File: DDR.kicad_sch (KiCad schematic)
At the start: 62 parts, among them U1 XC7Z020-2CLG484I, U2 MT41K256M16TW, U3 TPS51200DRCR, U4 MT41K256M16TW

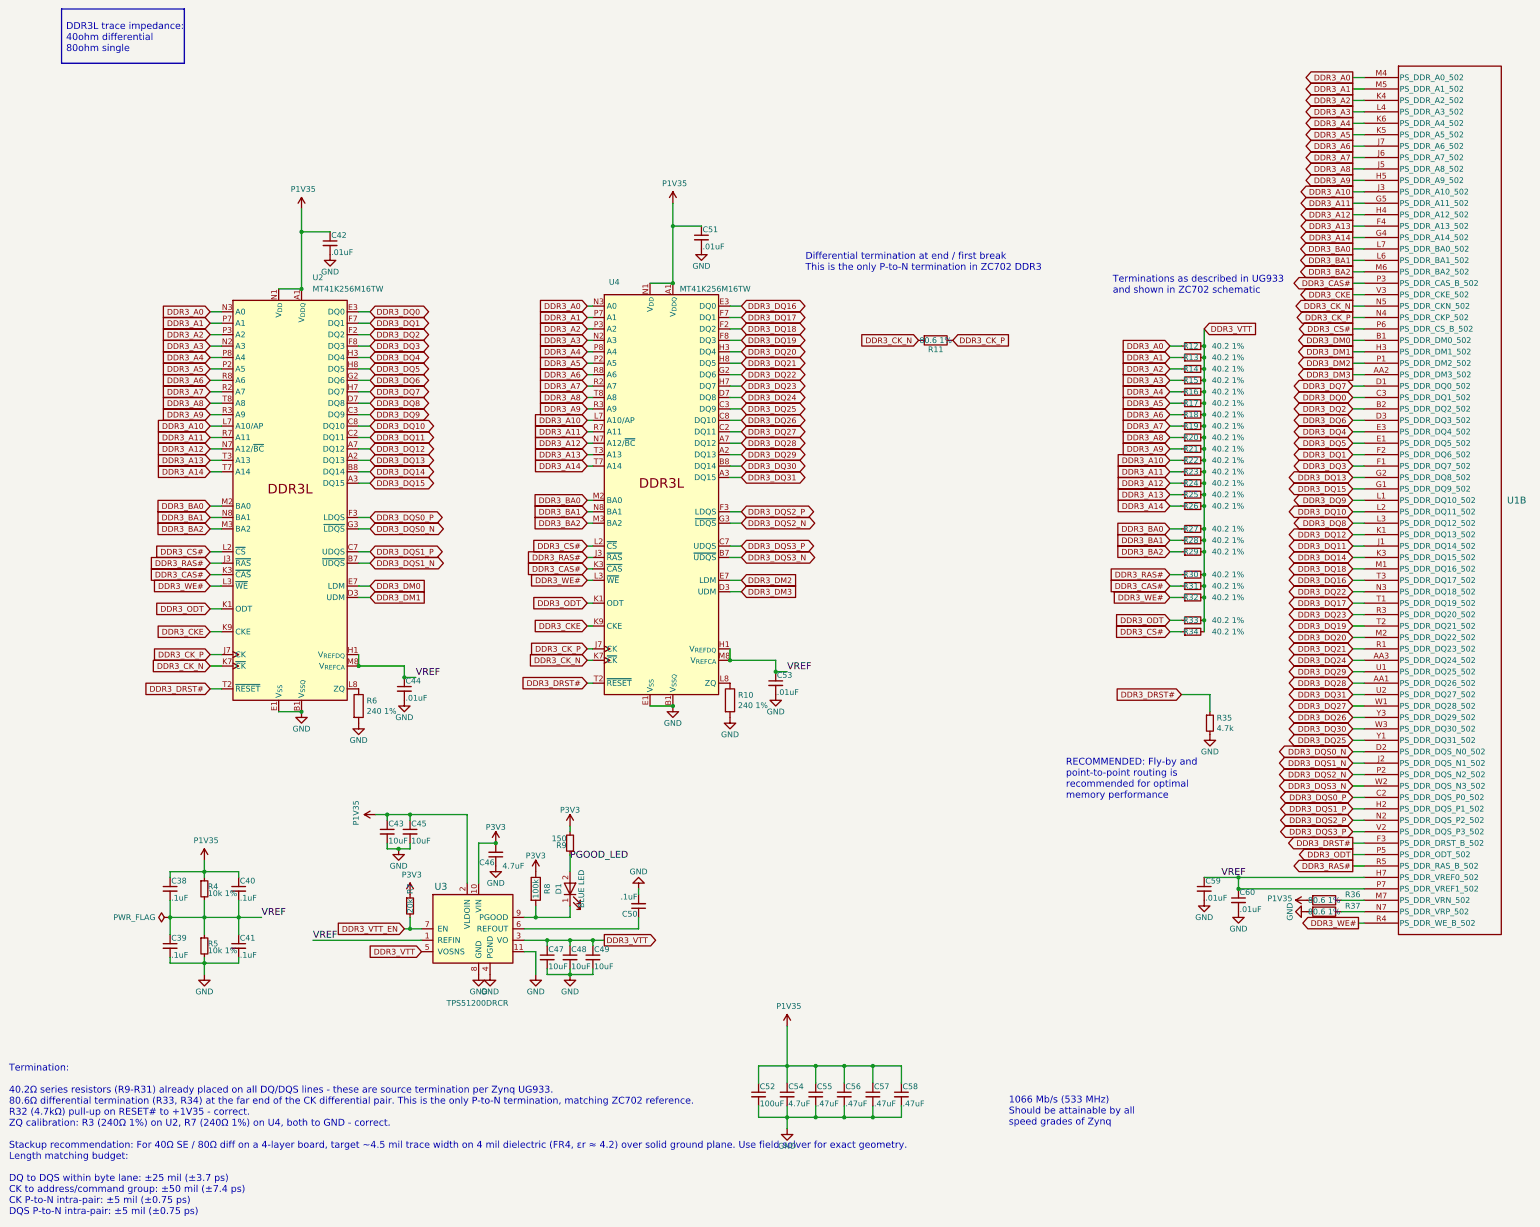
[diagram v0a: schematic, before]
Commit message: updated layouts, added motor
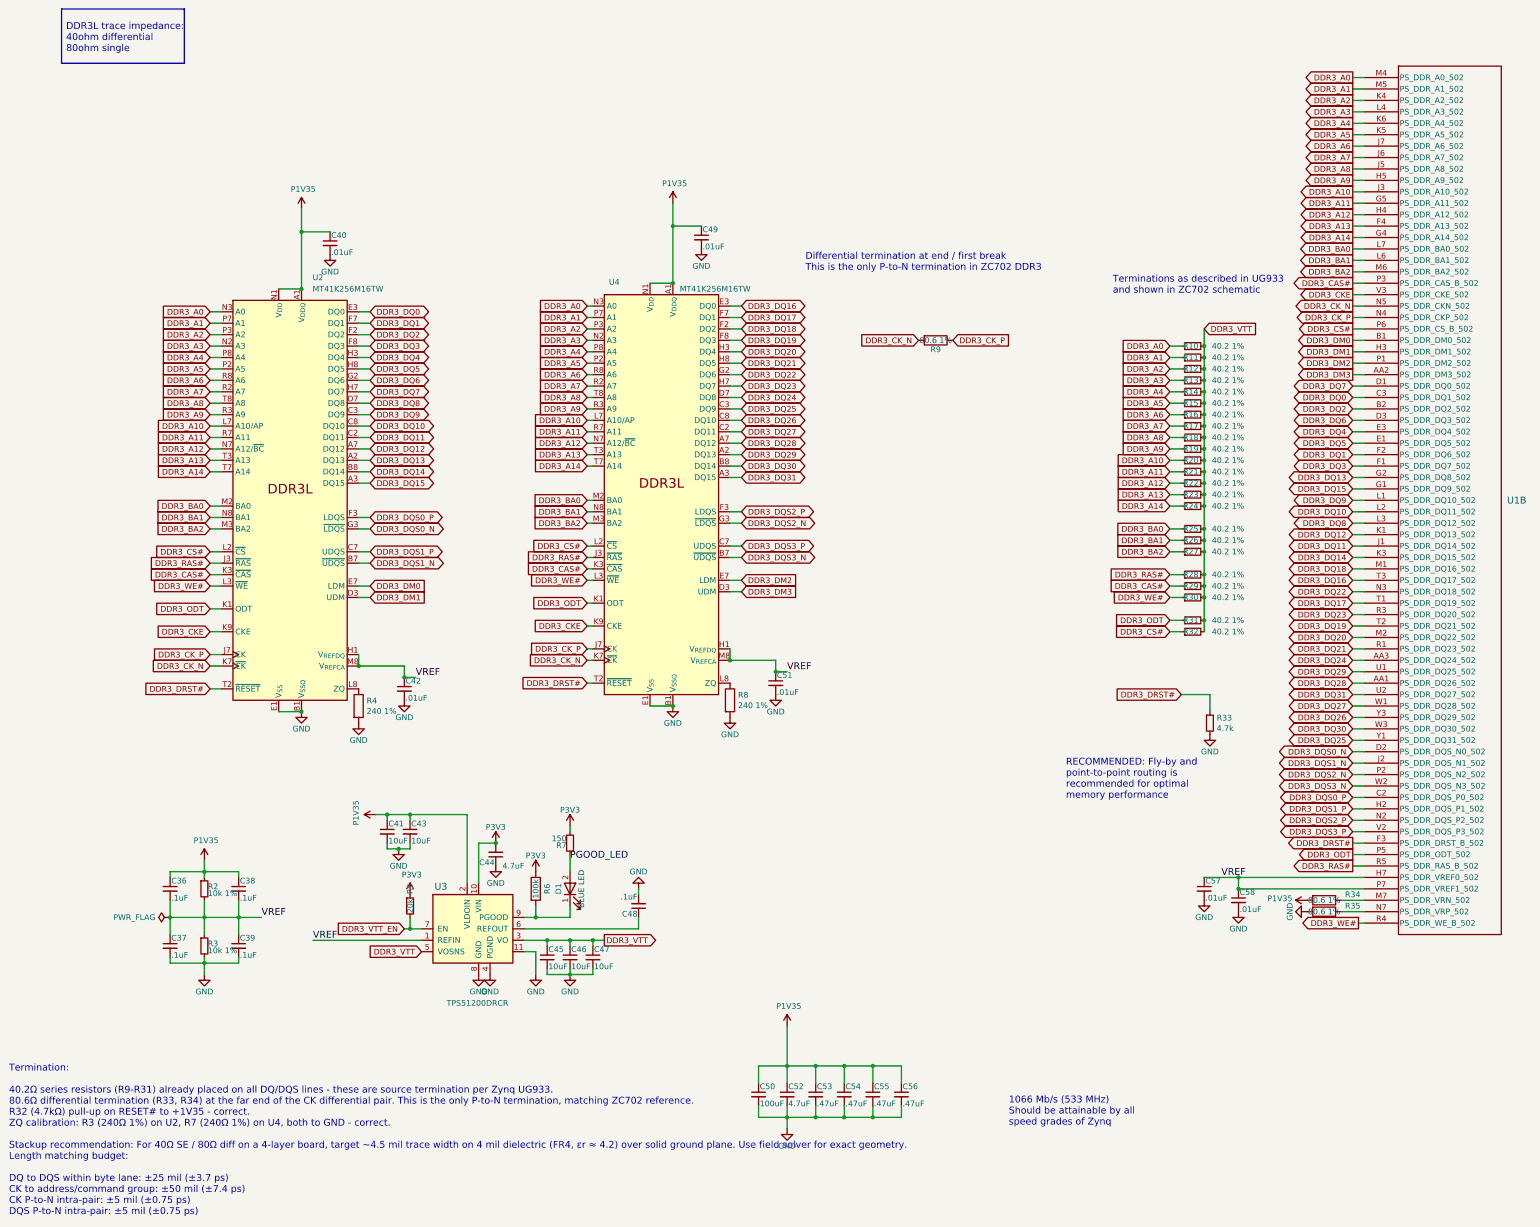
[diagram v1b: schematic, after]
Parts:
- renumbered C38 to C36, C39 to C37, C40 to C38, C41 to C39, C42 to C40, C43 to C41, C44 to C42, C45 to C43, C46 to C44, C47 to C45, C48 to C46, C49 to C47, C50 to C48, C51 to C49, C52 to C50, C53 to C51, C54 to C52, C55 to C53, C56 to C54, C57 to C55, C58 to C56, C59 to C57, C60 to C58, R12 to R10, R13 to R11, R14 to R12, R15 to R13, R16 to R14, R17 to R15, R18 to R16, R19 to R17, R20 to R18, R21 to R19, R4 to R2, R22 to R20, R23 to R21, R24 to R22, R25 to R23, R26 to R24, R27 to R25, R28 to R26, R29 to R27, R30 to R28, R31 to R29, R5 to R3, R32 to R30, R33 to R31, R34 to R32, R35 to R33, R36 to R34, R37 to R35, R6 to R4, R7 to R5, R8 to R6, R9 to R7, R10 to R8, R11 to R9

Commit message: Changes to layout pins
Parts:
- D1: symbol DFTBoard-rescue:LED- -> Device:LED
- U1: footprint DFTcustom:BGA-484_19.0x19.0mm_Layout22x22_P0.80mm_dia0.40mm -> FPGA:BGA-484_19.0x19.0mm_Layout22x22_P0.80mm_dia0.40mm
- U3: symbol tps51200DRCR:TPS51200DRCR -> KiCAD_Library_Cooter:TPS51200DRCR
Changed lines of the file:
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@@
 	(wire
 		(pts
-			(xy 81.28 223.52) (xy 105.41 223.52)
+			(xy 76.2 223.52) (xy 105.41 223.52)
 		)
 		(stroke
@@
 	)
 	(label "VREF"
-		(at 81.28 223.52 0)
+		(at 76.2 223.52 0)
 		(effects
 			(font
@@
 		(dnp no)
 		(property "Reference" "R9"
-			(at 219.71 92.202 90)
+			(at 219.71 88.138 90)
 			(show_name no)
 			(do_not_autoplace no)
@@
 		)
 		(property "Value" "80.6 1%"
-			(at 219.71 90.17 90)
+			(at 219.71 92.202 90)
 			(show_name no)
 			(do_not_autoplace no)
@@
 	)
 	(symbol
-		(lib_id "tps51200DRCR:TPS51200DRCR")
+		(lib_id "KiCAD_Library_Cooter:TPS51200DRCR")
 		(at 118.11 220.98 0)
 		(unit 1)
@@
 	)
 	(symbol
-		(lib_id "DFTBoard-rescue:LED-")
+		(lib_id "Device:LED")
 		(at 138.43 212.09 90)
 		(unit 1)
@@
 			)
 		)
-		(property "Description" ""
+		(property "Description" "Light emitting diode"
+			(at 138.43 212.09 0)
+			(hide yes)
+			(show_name no)
+			(do_not_autoplace no)
+			(effects
+				(font
+					(size 1.27 1.27)
+				)
+			)
+		)
+		(property "Sim.Pins" "1=K 2=A"
 			(at 138.43 212.09 0)
 			(hide yes)
@@
 		(fields_autoplaced yes)
 		(property "Reference" "U1"
-			(at 346.71 125.73 0)
+			(at 346.71 125.7299 0)
 			(show_name no)
 			(do_not_autoplace no)
@@
 			)
 		)
-		(property "Footprint" "DFTcustom:BGA-484_19.0x19.0mm_Layout22x22_P0.80mm_dia0.40mm"
+		(property "Footprint" "FPGA:BGA-484_19.0x19.0mm_Layout22x22_P0.80mm_dia0.40mm"
 			(at 274.32 -20.32 0)
 			(hide yes)
